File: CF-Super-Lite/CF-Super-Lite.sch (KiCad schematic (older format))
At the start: 12 parts, among them J1 IDE_CONNECTOR, J2 CF Adapter Power, J3 Bus_ISA_8bit, SW1 DIP Switch x3 or x4, U1 BIOS FLASH, U2 74HCT245, U3 GAL22V10

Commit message: CF-Super-Lite: Swap dip switch and resistor array for jumper block.
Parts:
- removed RN1: 10K, Resistor_THT:R_Array_SIP5, symbol Device:R_Network04
- removed SW1: DIP Switch x3 or x4, Button_Switch_THT:SW_DIP_SPSTx04_Slide_9.78x12.34mm_W7.62mm_P2.54mm, symbol Switch:SW_DIP_x04
- added J3: Jumpers, 00Custom:PinHeader_3x03_P2.54mm_Vertical, symbol 00Common:Conn_03x03
- renumbered J3 to J4
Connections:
- net ATA_ADDR_JUMPER: now also J3.5 (Pin_5)
- net GND: now also J3.1 (Pin_1), J3.4 (Pin_4), J3.7 (Pin_7)
- net ROM_ADDR_JUMPER: now also J3.8 (Pin_8)
- net V20_JUMPER: now also J3.2 (Pin_2)
- net VCC: now also J3.3 (Pin_4), J3.6 (Pin_6), J3.9 (Pin_9)
- no-connect marks 42 -> 39
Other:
- moved on the sheet: U1
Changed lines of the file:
@@
 	3650 950  1050 950
 $Comp
-L 00Common:Bus_ISA_8bit J3
+L 00Common:Bus_ISA_8bit J4
 U 1 1 6039F90B
 P 2500 2900
-F 0 "J3" H 2500 4667 50  0000 C CNN
+F 0 "J4" H 2500 4667 50  0000 C CNN
 F 1 "Bus_ISA_8bit" H 2500 4576 50  0000 C CNN
 F 2 "00Custom:BUS_XT" H 2500 2900 50  0001 C CNN
@@
 L Memory_Flash:SST39SF040 U1
 U 1 1 603B5177
-P 7400 4300
-F 0 "U1" H 7400 5871 50  0000 C CNN
-F 1 "BIOS FLASH" H 7400 5780 50  0000 C CNN
-F 2 "Package_DIP:DIP-32_W15.24mm_Socket" H 7400 4600 50  0001 C CNN
-F 3 "http://ww1.microchip.com/downloads/en/DeviceDoc/25022B.pdf" H 7400 4600 50  0001 C CNN
-F 4 "SST39SF010, SST39SF020, SST39SF040 or similar" H 7400 5689 50  0000 C CNN "Note"
-	1    7400 4300
+P 7400 4800
+F 0 "U1" H 7400 6371 50  0000 C CNN
+F 1 "BIOS FLASH" H 7400 6280 50  0000 C CNN
+F 2 "Package_DIP:DIP-32_W15.24mm_Socket" H 7400 5100 50  0001 C CNN
+F 3 "http://ww1.microchip.com/downloads/en/DeviceDoc/25022B.pdf" H 7400 5100 50  0001 C CNN
+F 4 "SST39SF010, SST39SF020, SST39SF040 or similar" H 7400 6189 50  0000 C CNN "Note"
+	1    7400 4800
 	1    0    0    -1
 $EndComp
@@
 	1    0    0    -1
 $EndComp
-Text GLabel 6800 3100 0    50   Input ~ 0
+Text GLabel 6800 3600 0    50   Input ~ 0
 A00
-Text GLabel 6800 3200 0    50   Input ~ 0
+Text GLabel 6800 3700 0    50   Input ~ 0
 A01
-Text GLabel 6800 3300 0    50   Input ~ 0
+Text GLabel 6800 3800 0    50   Input ~ 0
 A02
-Text GLabel 6800 3400 0    50   Input ~ 0
+Text GLabel 6800 3900 0    50   Input ~ 0
 A03
-Text GLabel 6800 3500 0    50   Input ~ 0
+Text GLabel 6800 4000 0    50   Input ~ 0
 A04
-Text GLabel 6800 3600 0    50   Input ~ 0
+Text GLabel 6800 4100 0    50   Input ~ 0
 A05
-Text GLabel 6800 3700 0    50   Input ~ 0
+Text GLabel 6800 4200 0    50   Input ~ 0
 A06
-Text GLabel 6800 3800 0    50   Input ~ 0
+Text GLabel 6800 4300 0    50   Input ~ 0
 A07
-Text GLabel 6800 3900 0    50   Input ~ 0
+Text GLabel 6800 4400 0    50   Input ~ 0
 A08
-Text GLabel 6800 4000 0    50   Input ~ 0
+Text GLabel 6800 4500 0    50   Input ~ 0
 A09
-Text GLabel 6800 4100 0    50   Input ~ 0
+Text GLabel 6800 4600 0    50   Input ~ 0
 A10
-Text GLabel 6800 4200 0    50   Input ~ 0
+Text GLabel 6800 4700 0    50   Input ~ 0
 A11
-Text GLabel 6800 4300 0    50   Input ~ 0
+Text GLabel 6800 4800 0    50   Input ~ 0
 A12
-Text GLabel 6800 4400 0    50   Input ~ 0
+Text GLabel 6800 4900 0    50   Input ~ 0
 A13
 Wire Wire Line
-	6800 4900 6400 4900
-Wire Wire Line
-	6400 4900 6400 5700
+	6800 5400 6400 5400
+Wire Wire Line
+	6400 5400 6400 6100
 $Comp
 L power:GND #PWR0112
 U 1 1 6042FC5C
-P 6400 5700
-F 0 "#PWR0112" H 6400 5450 50  0001 C CNN
-F 1 "GND" H 6405 5527 50  0000 C CNN
-F 2 "" H 6400 5700 50  0001 C CNN
-F 3 "" H 6400 5700 50  0001 C CNN
-	1    6400 5700
-	1    0    0    -1
-$EndComp
-Text GLabel 6800 5100 0    39   Input ~ 0
+P 6400 6100
+F 0 "#PWR0112" H 6400 5850 50  0001 C CNN
+F 1 "GND" H 6405 5927 50  0000 C CNN
+F 2 "" H 6400 6100 50  0001 C CNN
+F 3 "" H 6400 6100 50  0001 C CNN
+	1    6400 6100
+	1    0    0    -1
+$EndComp
+Text GLabel 6800 5600 0    39   Input ~ 0
 ~MEMW
-Text GLabel 6800 5400 0    39   Input ~ 0
+Text GLabel 6800 5900 0    39   Input ~ 0
 ~MEMR
-Text GLabel 6800 5300 0    39   Input ~ 0
+Text GLabel 6800 5800 0    39   Input ~ 0
 ~CE~_BIOS
-Text GLabel 8000 3100 2    50   Input ~ 0
+Text GLabel 8000 3600 2    50   Input ~ 0
 D0_BUF
-Text GLabel 8000 3200 2    50   Input ~ 0
+Text GLabel 8000 3700 2    50   Input ~ 0
 D1_BUF
-Text GLabel 8000 3300 2    50   Input ~ 0
+Text GLabel 8000 3800 2    50   Input ~ 0
 D2_BUF
-Text GLabel 8000 3400 2    50   Input ~ 0
+Text GLabel 8000 3900 2    50   Input ~ 0
 D3_BUF
-Text GLabel 8000 3500 2    50   Input ~ 0
+Text GLabel 8000 4000 2    50   Input ~ 0
 D4_BUF
-Text GLabel 8000 3600 2    50   Input ~ 0
+Text GLabel 8000 4100 2    50   Input ~ 0
 D5_BUF
-Text GLabel 8000 3700 2    50   Input ~ 0
+Text GLabel 8000 4200 2    50   Input ~ 0
 D6_BUF
-Text GLabel 8000 3800 2    50   Input ~ 0
+Text GLabel 8000 4300 2    50   Input ~ 0
 D7_BUF
 Text GLabel 5050 2000 2    39   Input ~ 0
@@
 Text GLabel 4050 2300 0    50   Input ~ 0
 A15
-Text GLabel 6800 4600 0    50   Input ~ 0
+Text GLabel 6800 5100 0    50   Input ~ 0
 V20_JUMPER
 Wire Wire Line
-	6800 4700 6400 4700
-Wire Wire Line
-	6400 4700 6400 4800
-Connection ~ 6400 4900
-Wire Wire Line
-	6800 4800 6400 4800
-Connection ~ 6400 4800
-Wire Wire Line
-	6400 4800 6400 4900
-Text GLabel 6800 4500 0    50   Input ~ 0
+	6800 5200 6400 5200
+Wire Wire Line
+	6400 5200 6400 5300
+Connection ~ 6400 5400
+Wire Wire Line
+	6800 5300 6400 5300
+Connection ~ 6400 5300
+Wire Wire Line
+	6400 5300 6400 5400
+Text GLabel 6800 5000 0    50   Input ~ 0
 ATA_ADDR_JUMPER
 $Comp
@@
 Text Notes 3800 1100 0    79   ~ 0
 DECODING
-Text Notes 6050 2700 0    79   ~ 0
+Text Notes 6050 3200 0    79   ~ 0
 BIOS
 Text Notes 8600 1100 0    79   ~ 0
@@
 	3750 950  3750 3300
 Wire Notes Line
-	8450 2550 8450 6000
-Wire Notes Line
-	8450 6000 6000 6000
-Wire Notes Line
-	6000 2550 6000 6000
-Wire Notes Line
-	6000 2550 8450 2550
-Wire Notes Line
-	6000 2450 6000 950
-Wire Notes Line
-	8450 2450 6000 2450
-Wire Notes Line
-	8450 950  8450 2450
+	8450 3050 8450 6400
+Wire Notes Line
+	8450 6400 6000 6400
+Wire Notes Line
+	6000 3050 6000 6400
+Wire Notes Line
+	6000 3050 8450 3050
+Wire Notes Line
+	6000 2950 6000 950
+Wire Notes Line
+	8450 2950 6000 2950
+Wire Notes Line
+	8450 950  8450 2950
 Wire Notes Line
 	6000 950  8450 950
 Text Notes 6050 1100 0    79   ~ 0
 JUMPERS
-Wire Wire Line
-	7200 1750 6950 1750
-Connection ~ 7200 1750
-Wire Wire Line
-	7200 2050 7200 1750
-Wire Wire Line
-	7300 2050 7200 2050
-Wire Wire Line
-	7100 1650 7650 1650
-Connection ~ 7100 1650
-Wire Wire Line
-	7100 2150 7100 1650
-Wire Wire Line
-	7200 2150 7100 2150
-Wire Wire Line
-	7000 1550 6950 1550
-Connection ~ 7000 1550
-Wire Wire Line
-	7000 2250 7000 1550
-Wire Wire Line
-	7100 2250 7000 2250
-Text GLabel 7300 2050 2    50   Input ~ 0
-V20_JUMPER
-Text GLabel 7200 2150 2    50   Input ~ 0
-ATA_ADDR_JUMPER
-Text GLabel 7100 2250 2    50   Input ~ 0
-ROM_ADDR_JUMPER
-NoConn ~ 6350 1850
-NoConn ~ 6950 1850
-NoConn ~ 7650 1850
-$Comp
-L Switch:SW_DIP_x04 SW1
-U 1 1 6040A722
-P 6650 1750
-F 0 "SW1" H 6650 2217 50  0000 C CNN
-F 1 "DIP Switch x3 or x4" H 6650 2126 50  0000 C CNN
-F 2 "Button_Switch_THT:SW_DIP_SPSTx04_Slide_9.78x12.34mm_W7.62mm_P2.54mm" H 6650 1750 50  0001 C CNN
-F 3 "~" H 6650 1750 50  0001 C CNN
-	1    6650 1750
-	1    0    0    -1
-$EndComp
-Wire Wire Line
-	7650 1750 7200 1750
-Wire Wire Line
-	6950 1650 7100 1650
-Wire Wire Line
-	7650 1550 7000 1550
-$Comp
-L Device:R_Network04 RN1
-U 1 1 603F8484
-P 7850 1750
-F 0 "RN1" V 7433 1750 50  0000 C CNN
-F 1 "10K" V 7524 1750 50  0000 C CNN
-F 2 "Resistor_THT:R_Array_SIP5" V 8125 1750 50  0001 C CNN
-F 3 "http://www.vishay.com/docs/31509/csc.pdf" H 7850 1750 50  0001 C CNN
-	1    7850 1750
-	0    1    1    0
-$EndComp
-Wire Wire Line
-	8150 1550 8150 1950
-Wire Wire Line
-	8050 1550 8150 1550
-Wire Wire Line
-	6200 1650 6200 1750
-Connection ~ 6200 1650
-Wire Wire Line
-	6350 1650 6200 1650
-Connection ~ 6200 1550
-Wire Wire Line
-	6200 1750 6350 1750
-Wire Wire Line
-	6200 1550 6200 1650
-Wire Wire Line
-	6200 1550 6200 1450
-Wire Wire Line
-	6350 1550 6200 1550
-$Comp
-L power:VCC #PWR0114
-U 1 1 603EA922
-P 6200 1450
-F 0 "#PWR0114" H 6200 1300 50  0001 C CNN
-F 1 "VCC" H 6215 1623 50  0000 C CNN
-F 2 "" H 6200 1450 50  0001 C CNN
-F 3 "" H 6200 1450 50  0001 C CNN
-	1    6200 1450
-	1    0    0    -1
-$EndComp
-$Comp
-L power:GND #PWR0113
-U 1 1 603D46A8
-P 8150 1950
-F 0 "#PWR0113" H 8150 1700 50  0001 C CNN
-F 1 "GND" H 8155 1777 50  0000 C CNN
-F 2 "" H 8150 1950 50  0001 C CNN
-F 3 "" H 8150 1950 50  0001 C CNN
-	1    8150 1950
-	1    0    0    -1
-$EndComp
 NoConn ~ 9250 3250
 $Comp
@@
 Text GLabel 5050 2300 2    39   Input ~ 0
 ~MEMR
+$Comp
+L 00Common:Conn_03x03 J3
+U 1 1 60676FBD
+P 7600 1550
+F 0 "J3" H 7780 1192 50  0000 L CNN
+F 1 "Jumpers" H 7780 1101 50  0000 L CNN
+F 2 "00Custom:PinHeader_3x03_P2.54mm_Vertical" H 7600 1550 50  0001 C CNN
+F 3 "~" H 7600 1550 50  0001 C CNN
+	1    7600 1550
+	1    0    0    -1
+$EndComp
+$Comp
+L power:GND #PWR0104
+U 1 1 6067888C
+P 7300 2550
+F 0 "#PWR0104" H 7300 2300 50  0001 C CNN
+F 1 "GND" H 7305 2377 50  0000 C CNN
+F 2 "" H 7300 2550 50  0001 C CNN
+F 3 "" H 7300 2550 50  0001 C CNN
+	1    7300 2550
+	1    0    0    -1
+$EndComp
+$Comp
+L power:VCC #PWR0105
+U 1 1 60683761
+P 7200 1350
+F 0 "#PWR0105" H 7200 1200 50  0001 C CNN
+F 1 "VCC" H 7215 1523 50  0000 C CNN
+F 2 "" H 7200 1350 50  0001 C CNN
+F 3 "" H 7200 1350 50  0001 C CNN
+	1    7200 1350
+	1    0    0    -1
+$EndComp
+Text GLabel 7100 2350 0    50   Input ~ 0
+ROM_ADDR_JUMPER
+Text GLabel 7100 1950 0    50   Input ~ 0
+ATA_ADDR_JUMPER
+Text GLabel 7100 1550 0    50   Input ~ 0
+V20_JUMPER
+Wire Wire Line
+	7100 1550 7400 1550
+Wire Wire Line
+	7400 1950 7100 1950
+Wire Wire Line
+	7100 2350 7400 2350
+Wire Wire Line
+	7300 1450 7300 1850
+Wire Wire Line
+	7200 1350 7200 1650
+Wire Wire Line
+	7400 1450 7300 1450
+Wire Wire Line
+	7400 1850 7300 1850
+Connection ~ 7300 1850
+Wire Wire Line
+	7300 1850 7300 2250
+Wire Wire Line
+	7400 2250 7300 2250
+Connection ~ 7300 2250
+Wire Wire Line
+	7300 2250 7300 2550
+Wire Wire Line
+	7400 2450 7200 2450
+Wire Wire Line
+	7400 2050 7200 2050
+Connection ~ 7200 2050
+Wire Wire Line
+	7200 2050 7200 2450
+Wire Wire Line
+	7400 1650 7200 1650
+Connection ~ 7200 1650
+Wire Wire Line
+	7200 1650 7200 2050
 $EndSCHEMATC

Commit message: CF-Super-Line: Swap two GAL pins to match CD-Clock-Combo.
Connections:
- net RESET: now also U3.17 (IO7); no longer U3.18 (IO6)
- net ~CE~_BIOS: now also U3.18 (IO6); no longer U3.17 (IO7)
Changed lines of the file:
@@
 Text GLabel 5050 2400 2    39   Input ~ 0
 ~RESET
-Text GLabel 5050 2200 2    39   Input ~ 0
+Text GLabel 5050 2100 2    39   Input ~ 0
 ~CE~_BIOS
 Text GLabel 5050 2500 2    39   Input ~ 0
@@
 NoConn ~ 2000 2000
 NoConn ~ 2000 2200
-Text GLabel 5050 2100 2    50   Input ~ 0
+Text GLabel 5050 2200 2    50   Input ~ 0
 RESET
 Wire Wire Line

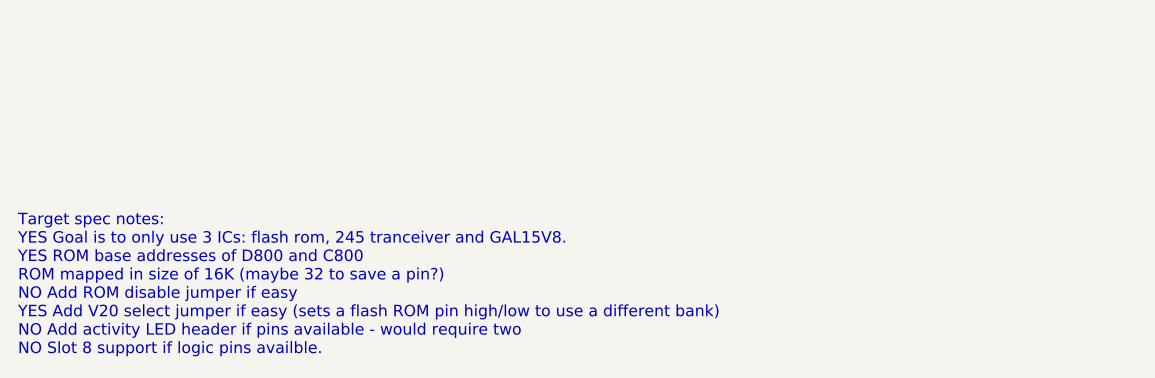
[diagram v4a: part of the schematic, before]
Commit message: CF-Super-Lite: Remove old notes from schematic.
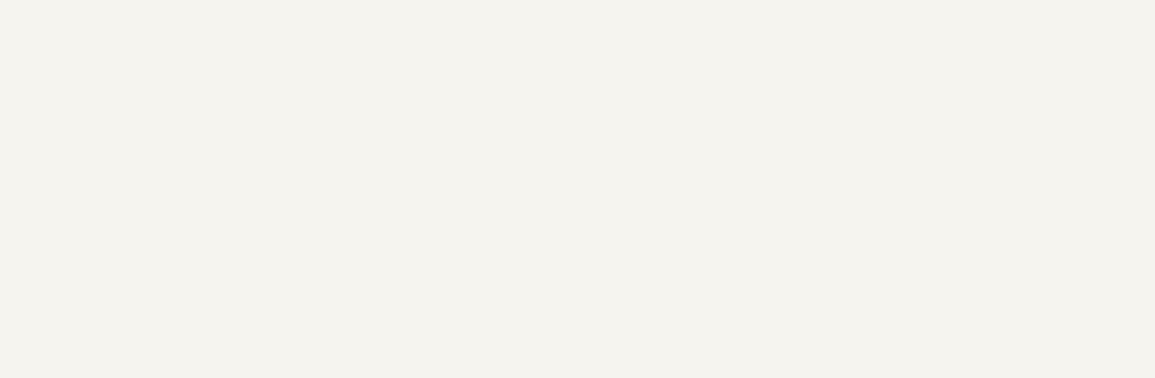
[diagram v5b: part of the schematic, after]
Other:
- note removed: "Target spec notes:\nYES Goal is to only use 3 ICs: flash rom, 245 tranceiver and GAL15V8.\nYES ROM base addresses of D800 and C800\nROM mapped in size of 16K (maybe 32 to save a pin?)\nNO Add ROM disable jumper if easy\nYES Add V20 select jumper if easy (sets a flash ROM pin high/low to use a different bank)\nNO Add activity LED header if pins available - would require two\nNO Slot 8 support if l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"
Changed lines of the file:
@@
 	1900 2300 1900 4400
 NoConn ~ 2000 2100
-Text Notes 550  7700 0    50   ~ 0
-Target spec notes:\nYES Goal is to only use 3 ICs: flash rom, 245 tranceiver and GAL15V8.\nYES ROM base addresses of D800 and C800\nROM mapped in size of 16K (maybe 32 to save a pin?)\nNO Add ROM disable jumper if easy\nYES Add V20 select jumper if easy (sets a flash ROM pin high/low to use a different bank)\nNO Add activity LED header if pins available - would require two\nNO Slot 8 support if logic pins availble.
 $Comp
 L Memory_Flash:SST39SF040 U1

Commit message: Fix location of CF adapter power for all boards that use it. Also the mounting holes in the schematic for the same boards. Finishing touches to Tandy 1000 Essentials.
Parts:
- added H1, H2, H3, H4: MountingHole_Pad, MountingHole:MountingHole_3.5mm_Pad, symbol Mechanical:MountingHole_Pad
- J2: footprint Connector_PinHeader_2.54mm:PinHeader_1x02_P2.54mm_Vertical -> Connector_PinSocket_2.54mm:PinSocket_1x01_P2.54mm_Vertical; symbol Connector_Generic:Conn_01x02 -> Connector_Generic:Conn_01x01
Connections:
- net GND: now also H1.1, H2.1, H3.1, H4.1; no longer J2.2 (Pin_2)
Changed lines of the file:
@@
 $EndComp
 $Comp
-L Connector_Generic:Conn_01x02 J2
+L Connector_Generic:Conn_01x01 J2
 U 1 1 603E8D26
 P 9450 4050
 F 0 "J2" H 9530 4042 50  0000 L CNN
 F 1 "CF Adapter Power" H 9530 3951 50  0000 L CNN
-F 2 "Connector_PinHeader_2.54mm:PinHeader_1x02_P2.54mm_Vertical" H 9450 4050 50  0001 C CNN
+F 2 "Connector_PinSocket_2.54mm:PinSocket_1x01_P2.54mm_Vertical" H 9450 4050 50  0001 C CNN
 F 3 "~" H 9450 4050 50  0001 C CNN
 	1    9450 4050
-	1    0    0    -1
-$EndComp
-$Comp
-L power:GND #PWR0123
-U 1 1 603E9698
-P 9250 4150
-F 0 "#PWR0123" H 9250 3900 50  0001 C CNN
-F 1 "GND" H 9255 3977 50  0000 C CNN
-F 2 "" H 9250 4150 50  0001 C CNN
-F 3 "" H 9250 4150 50  0001 C CNN
-	1    9250 4150
 	1    0    0    -1
 $EndComp
@@
 Wire Wire Line
 	7200 1650 7200 2050
+$Comp
+L Mechanical:MountingHole_Pad H1
+U 1 1 608FEC20
+P 9400 4600
+F 0 "H1" V 9354 4750 50  0000 L CNN
+F 1 "MountingHole_Pad" V 9445 4750 50  0000 L CNN
+F 2 "MountingHole:MountingHole_3.5mm_Pad" H 9400 4600 50  0001 C CNN
+F 3 "~" H 9400 4600 50  0001 C CNN
+	1    9400 4600
+	0    1    1    0
+$EndComp
+$Comp
+L Mechanical:MountingHole_Pad H2
+U 1 1 608FF3EA
+P 9400 4800
+F 0 "H2" V 9354 4950 50  0000 L CNN
+F 1 "MountingHole_Pad" V 9445 4950 50  0000 L CNN
+F 2 "MountingHole:MountingHole_3.5mm_Pad" H 9400 4800 50  0001 C CNN
+F 3 "~" H 9400 4800 50  0001 C CNN
+	1    9400 4800
+	0    1    1    0
+$EndComp
+$Comp
+L Mechanical:MountingHole_Pad H3
+U 1 1 608FF69F
+P 9400 5000
+F 0 "H3" V 9354 5150 50  0000 L CNN
+F 1 "MountingHole_Pad" V 9445 5150 50  0000 L CNN
+F 2 "MountingHole:MountingHole_3.5mm_Pad" H 9400 5000 50  0001 C CNN
+F 3 "~" H 9400 5000 50  0001 C CNN
+	1    9400 5000
+	0    1    1    0
+$EndComp
+$Comp
+L Mechanical:MountingHole_Pad H4
+U 1 1 608FF85E
+P 9400 5200
+F 0 "H4" V 9354 5350 50  0000 L CNN
+F 1 "MountingHole_Pad" V 9445 5350 50  0000 L CNN
+F 2 "MountingHole:MountingHole_3.5mm_Pad" H 9400 5200 50  0001 C CNN
+F 3 "~" H 9400 5200 50  0001 C CNN
+	1    9400 5200
+	0    1    1    0
+$EndComp
+Wire Wire Line
+	9300 4600 9200 4600
+Wire Wire Line
+	9200 4600 9200 4800
+Wire Wire Line
+	9300 5200 9200 5200
+Connection ~ 9200 5200
+Wire Wire Line
+	9200 5200 9200 5300
+Wire Wire Line
+	9300 5000 9200 5000
+Connection ~ 9200 5000
+Wire Wire Line
+	9200 5000 9200 5200
+Wire Wire Line
+	9300 4800 9200 4800
+Connection ~ 9200 4800
+Wire Wire Line
+	9200 4800 9200 5000
+$Comp
+L power:GND #PWR0113
+U 1 1 60909374
+P 9200 5300
+F 0 "#PWR0113" H 9200 5050 50  0001 C CNN
+F 1 "GND" H 9205 5127 50  0000 C CNN
+F 2 "" H 9200 5300 50  0001 C CNN
+F 3 "" H 9200 5300 50  0001 C CNN
+	1    9200 5300
+	1    0    0    -1
+$EndComp
 $EndSCHEMATC
